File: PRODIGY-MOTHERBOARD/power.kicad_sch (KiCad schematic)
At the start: 56 parts, among them J14 Barrel_Jack_MountingPin, Q2 PMOS, Q4 PMOS, U15 TPS22810DRV, U4 LM358, U5 TPS54331DR, U6 TPS54331DR

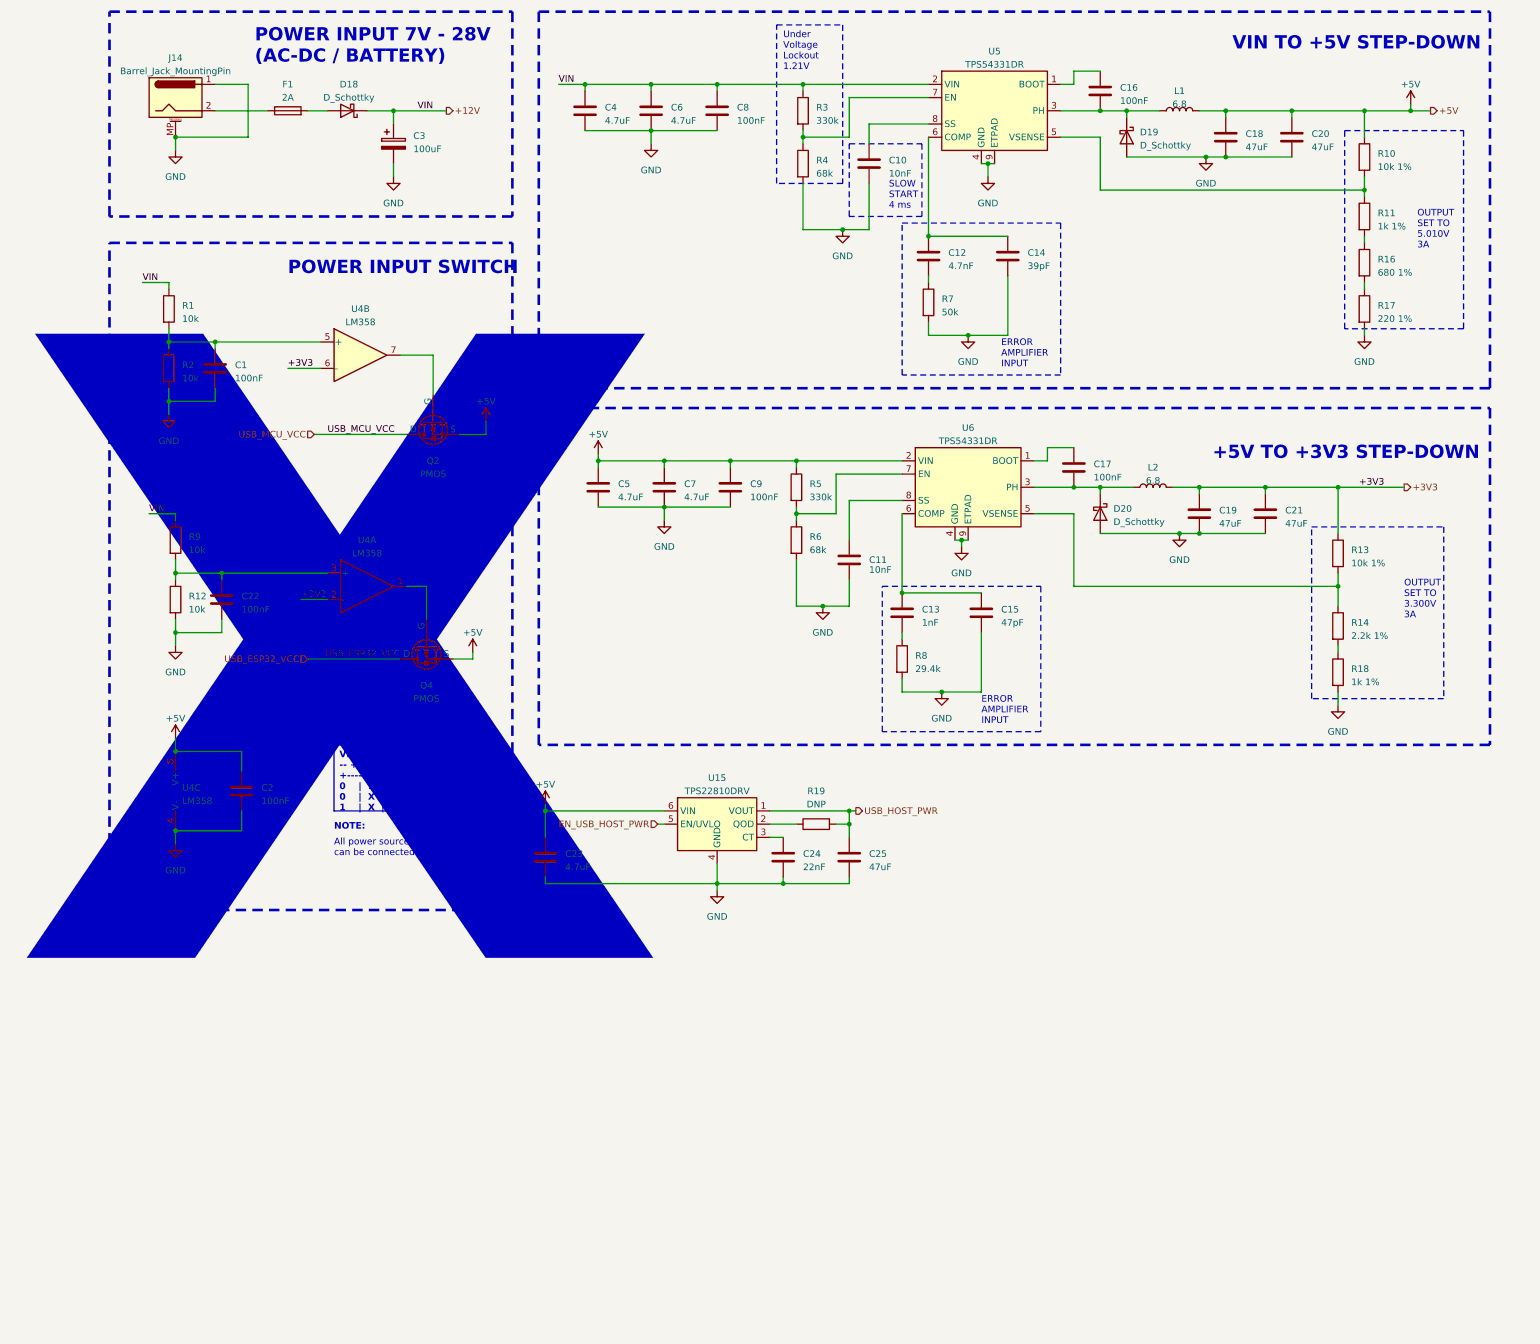
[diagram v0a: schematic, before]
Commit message: project restructure done. Hierarchical sheet done. Outputs/breakouts sheet done
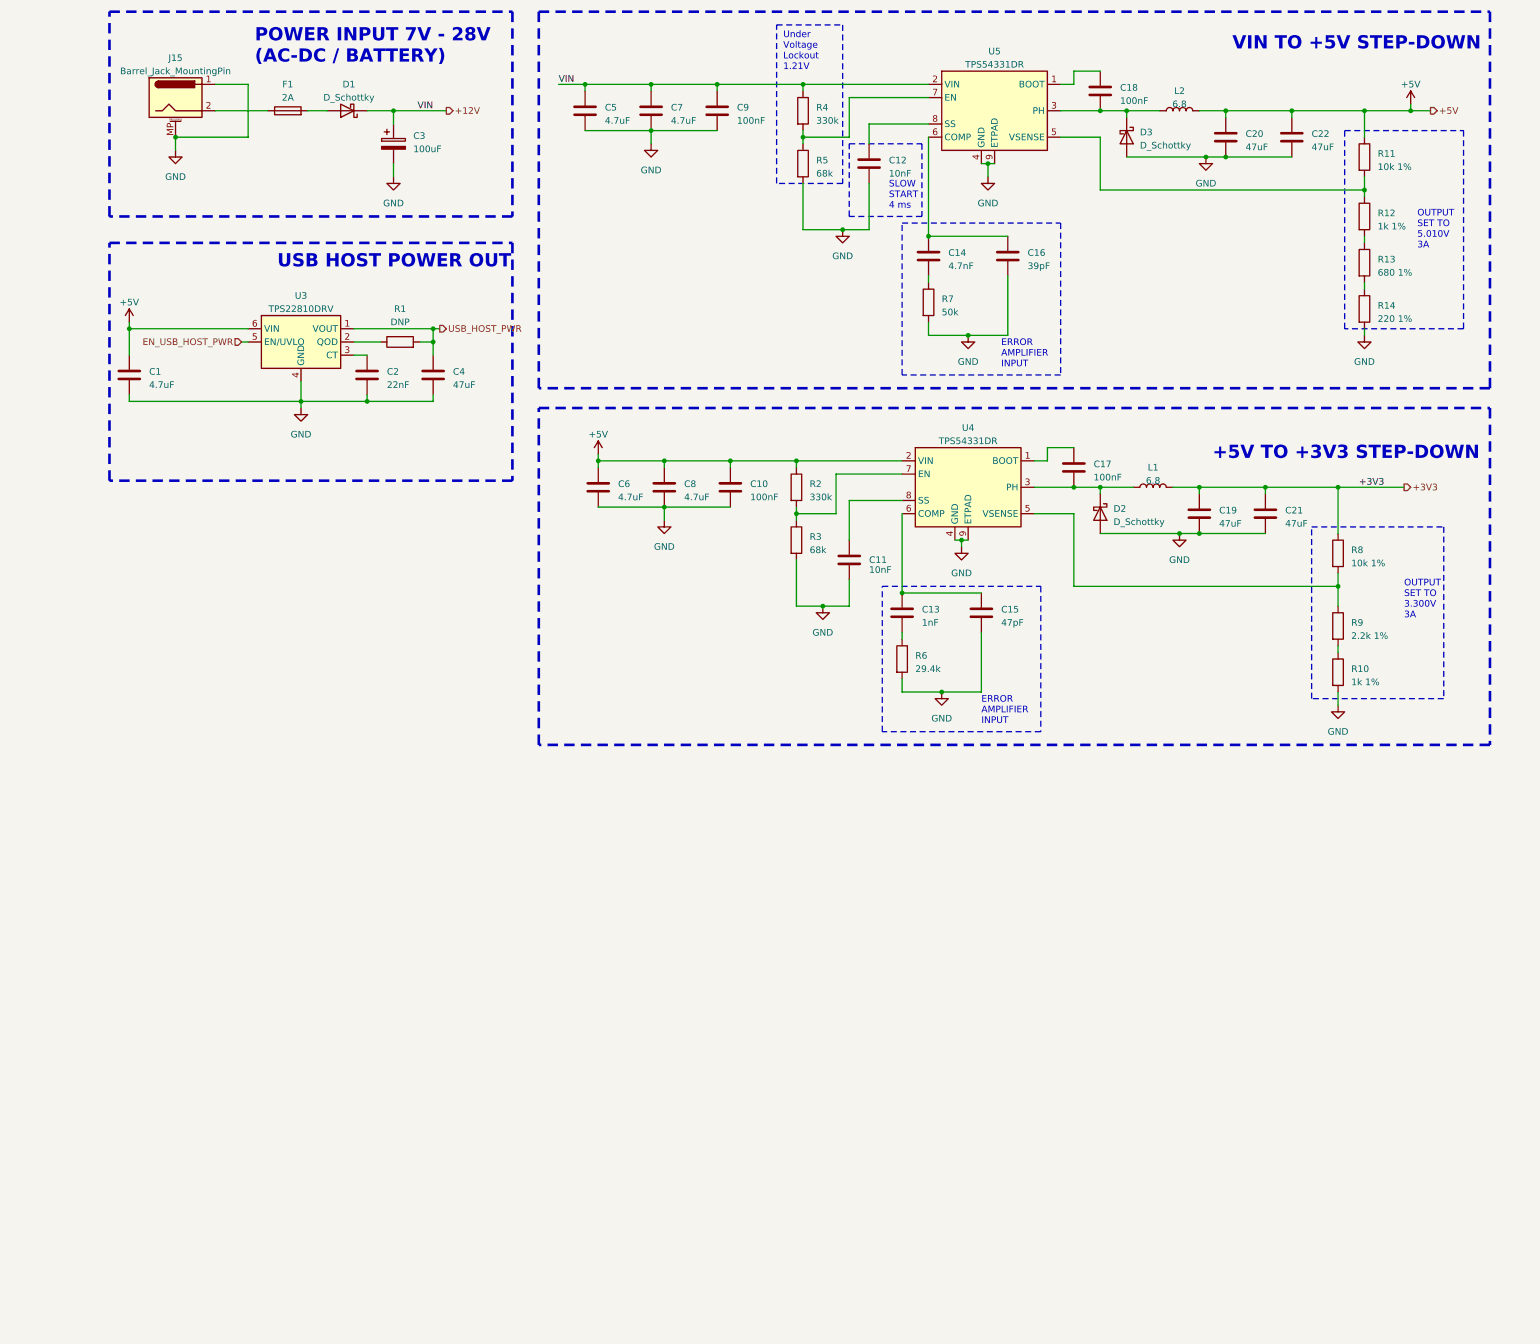
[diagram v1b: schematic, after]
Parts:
- removed C1, C2, C22: 100nF, Capacitor_SMD:C_0603_1608Metric, symbol Device:C
- removed Q2, Q4: PMOS, Package_TO_SOT_SMD:SOT-23, symbol Simulation_SPICE:PMOS
- removed R1, R12, R2, R9: 10k, Resistor_SMD:R_0603_1608Metric, symbol Device:R
- removed U4: LM358, Package_SO:SOIC-8_3.9x4.9mm_P1.27mm, symbol Amplifier_Operational:LM358
- renumbered C23 to C1, C9 to C10, C10 to C12, C12 to C14, C14 to C16, C16 to C18, C24 to C2, C18 to C20, C20 to C22, C25 to C4, C4 to C5, C5 to C6, C6 to C7, C7 to C8, C8 to C9, D18 to D1, D20 to D2, D19 to D3, J14 to J15, L2 to L1, L1 to L2, R19 to R1, R18 to R10, R10 to R11, R11 to R12, R16 to R13, R17 to R14, R5 to R2, R6 to R3, R3 to R4, R4 to R5, R8 to R6, R13 to R8, R14 to R9, U15 to U3, U6 to U4
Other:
- note added: "USB HOST POWER OUT"
- note removed: "All power sources can be connected simultaneously."
- note removed: "NOTE:"
- note removed: "POWER INPUT SWITCH"
- note removed: "POWER TRUTH TABLE"
- note removed: "X"
- moved on the sheet: C1, C2, C4, R1, U3

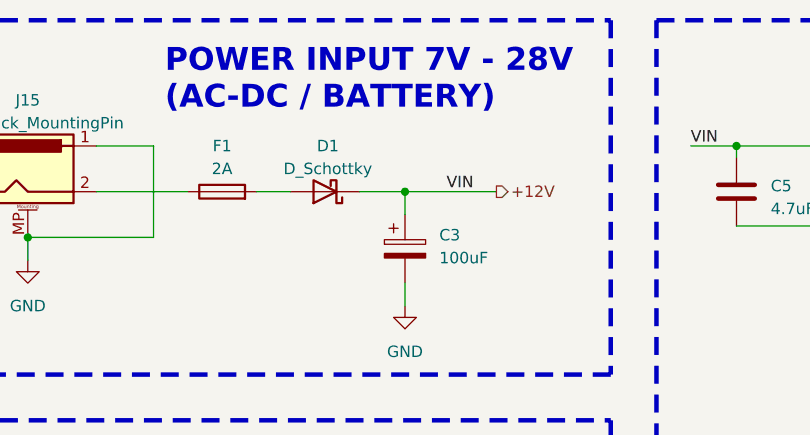
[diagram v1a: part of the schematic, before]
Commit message: Digital section done.
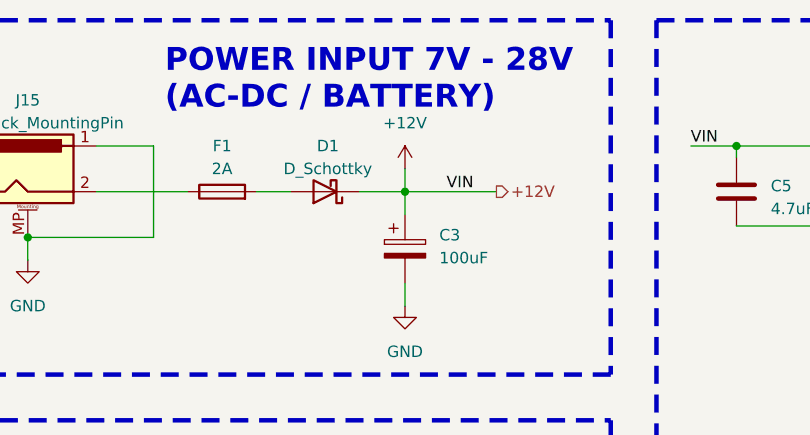
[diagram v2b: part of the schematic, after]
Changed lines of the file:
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@@
+	(wire
+		(pts
+			(xy 71.12 34.29) (xy 71.12 36.83)
+		)
+		(stroke
+			(width 0)
+			(type default)
+		)
+	)
 	(wire
 		(pts
@@
 					(unit 1)
 				)
+			)
+		)
+	)
+	(symbol
+		(lib_id "power:+12V")
+		(at 71.12 34.29 0)
+		(unit 1)
+		(exclude_from_sim no)
+		(in_bom yes)
+		(on_board yes)
+		(dnp no)
+		(fields_autoplaced yes)
+		(property "Reference" "#PWR0133"
+			(at 71.12 38.1 0)
+			(effects
+				(font
+					(size 1.27 1.27)
+				)
+				(hide yes)
+			)
+		)
+		(property "Value" "+12V"
+			(at 71.12 29.21 0)
+			(effects
+				(font
+					(size 1.27 1.27)
+				)
+			)
+		)
+		(property "Footprint" ""
+			(at 71.12 34.29 0)
+			(effects
+				(font
+					(size 1.27 1.27)
+				)
+				(hide yes)
+			)
+		)
+		(property "Datasheet" ""
+			(at 71.12 34.29 0)
+			(effects
+				(font
+					(size 1.27 1.27)
+				)
+				(hide yes)
+			)
+		)
+		(property "Description" "Power symbol creates a global label with name \"+12V\""
+			(at 71.12 34.29 0)
+			(effects
+				(font
+					(size 1.27 1.27)
+				)
+				(hide yes)
+			)
+		)
+		(pin "1"
+		)
+		(instances
+			(project "PRODIGY-MOTHERBOARD"
+				(path "/f1c25860-8989-4190-bd24-2491d23ca7d9/7df83d4f-8c4f-4445-bdae-bd2c13239983"
+					(reference "#PWR0133")
+					(unit 1)
+				)

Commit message: CAN schematic done
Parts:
- renumbered C5 to C10, C6 to C11, C7 to C12, C8 to C13, C9 to C14, C10 to C15, C11 to C16, C12 to C17, C13 to C18, C14 to C19, C15 to C20, C16 to C21, C17 to C22, C18 to C23, C19 to C24, C20 to C25, C21 to C26, C22 to C27, C1 to C6, C2 to C7, C3 to C8, C4 to C9, D1 to D4, D2 to D5, D3 to D6, J15 to J23, R2 to R10, R3 to R11, R4 to R12, R5 to R13, R6 to R14, R7 to R15, R8 to R16, R9 to R17, R10 to R18, R11 to R19, R12 to R20, R13 to R21, R14 to R22, R1 to R9, U3 to U5, U4 to U6, U5 to U7

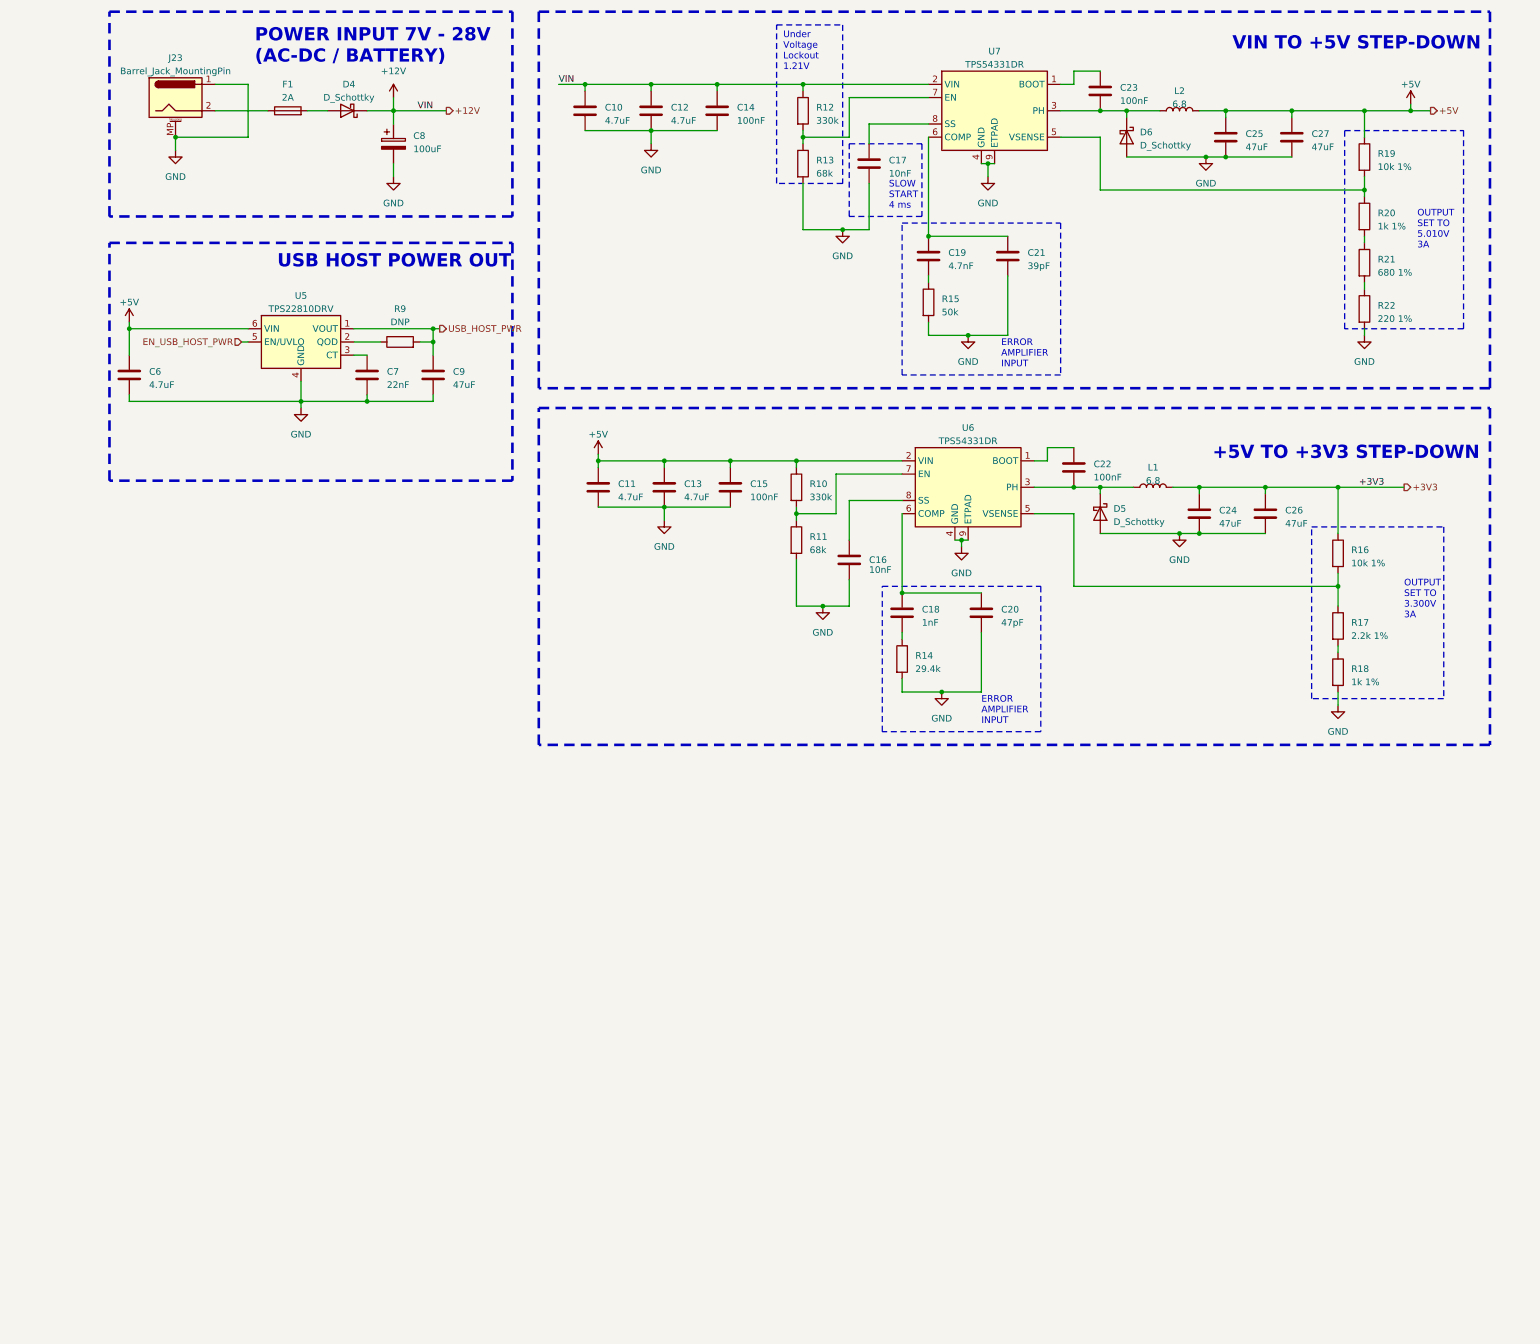
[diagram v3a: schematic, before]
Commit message: SPI NFC schematic done.
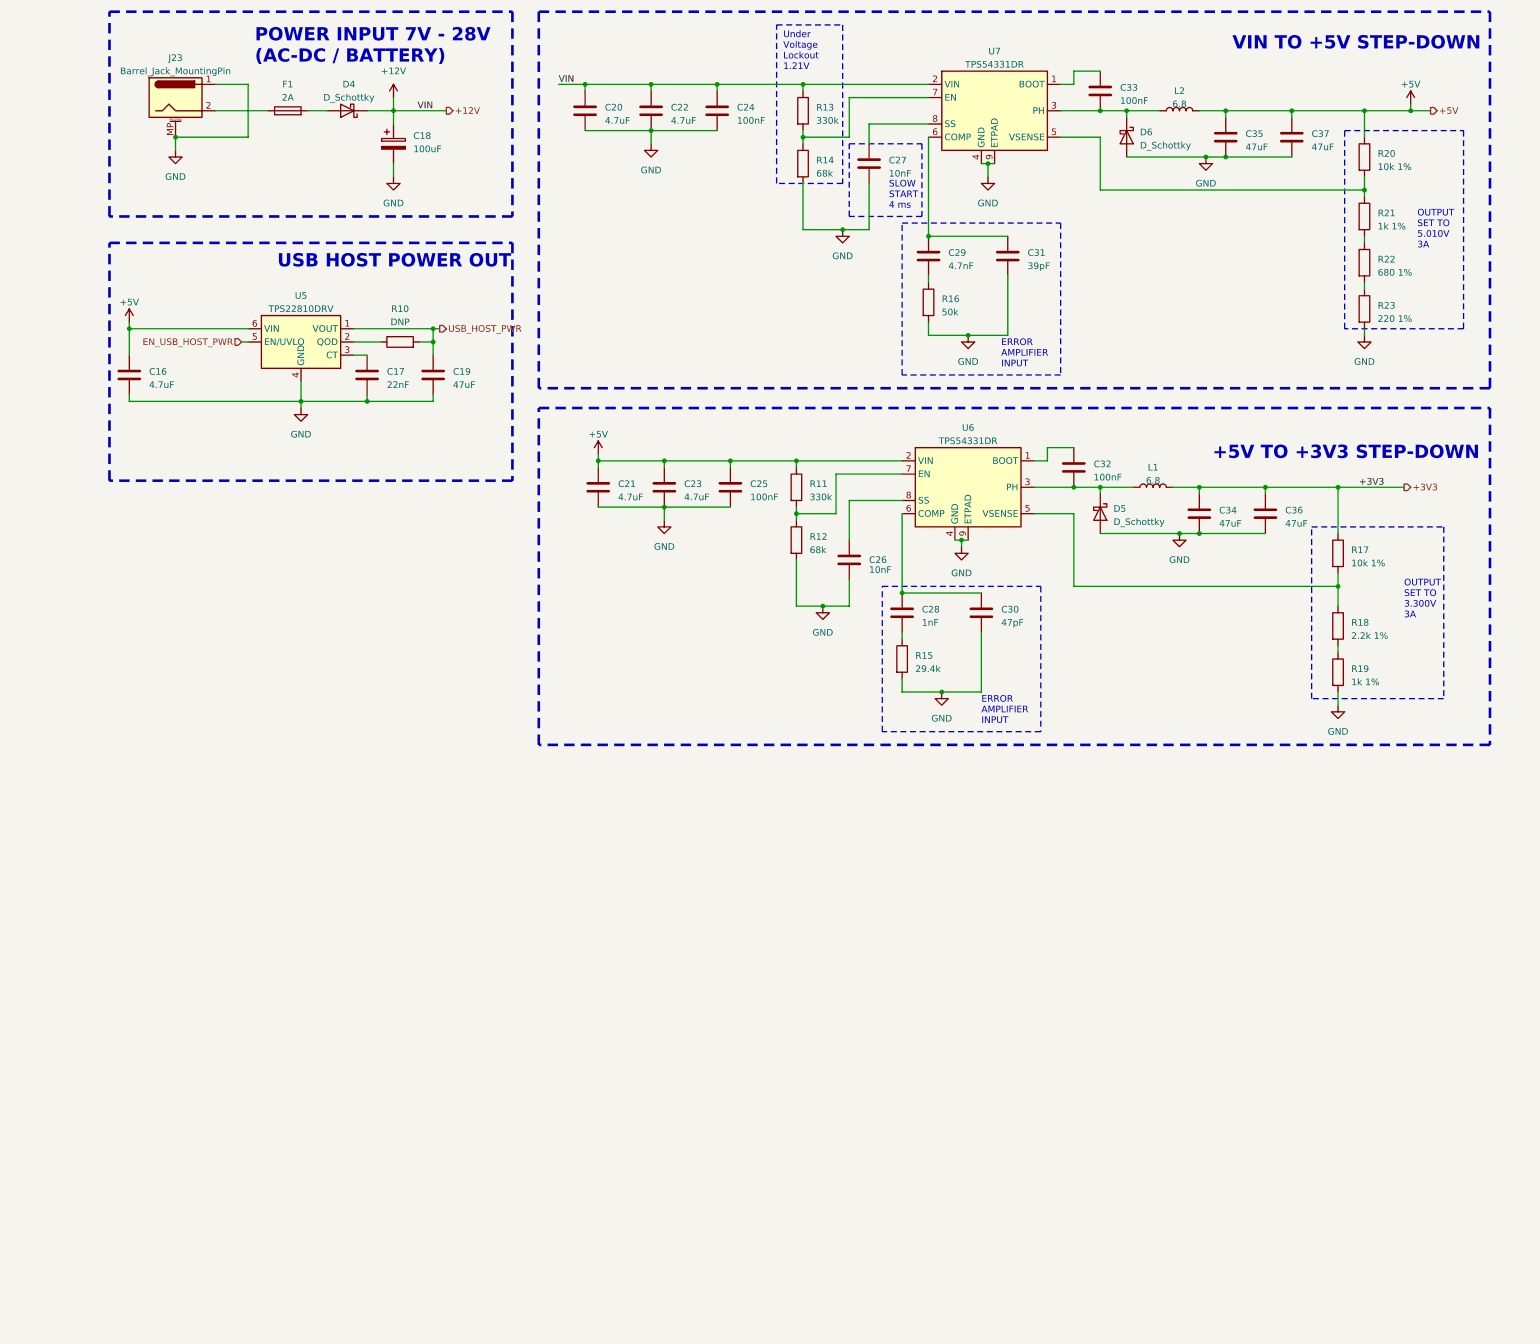
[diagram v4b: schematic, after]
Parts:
- renumbered C6 to C16, C7 to C17, C8 to C18, C9 to C19, C10 to C20, C11 to C21, C12 to C22, C13 to C23, C14 to C24, C15 to C25, C16 to C26, C17 to C27, C18 to C28, C19 to C29, C20 to C30, C21 to C31, C22 to C32, C23 to C33, C24 to C34, C25 to C35, C26 to C36, C27 to C37, R9 to R10, R10 to R11, R11 to R12, R12 to R13, R13 to R14, R14 to R15, R15 to R16, R16 to R17, R17 to R18, R18 to R19, R19 to R20, R20 to R21, R21 to R22, R22 to R23
